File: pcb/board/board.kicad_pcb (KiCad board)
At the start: 2 copper layers, 100 x 34 mm, 68 parts, among them J1 USB_C_Receptacle_USB2.0, J3 Micro_SD_Card_Det, J4 Conn_01x05_Male, J6 Conn_02x02_Top_Bottom, J7 Screw_Terminal_Speaker, Q1 DMG2305UX, SW6 BOOTSEL, U2 BQ25172, U3 TLV61070A, U4 XC6206P332MR, U5 MAX98357, U6 RP2040, U7 W25Q128JVS, Y1 X322512MSB4SI

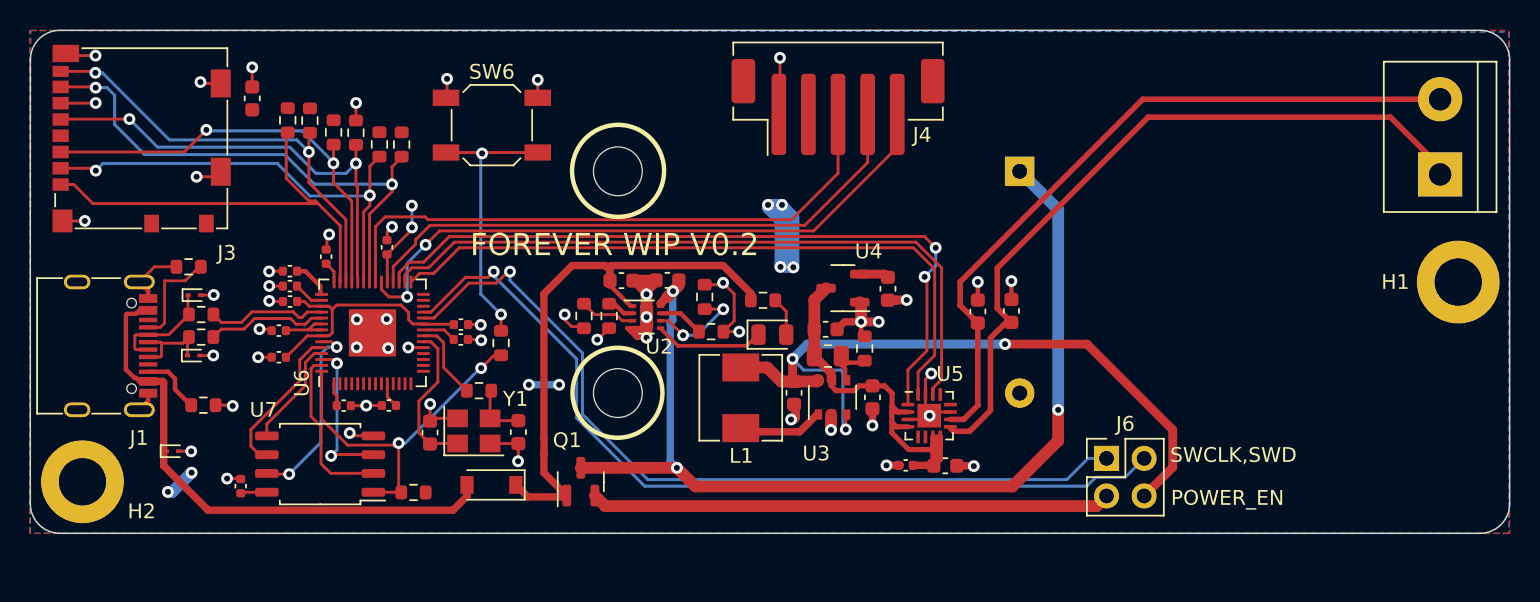
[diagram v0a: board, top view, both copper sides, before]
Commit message: Update readmes. Uncovered I2C bug :(
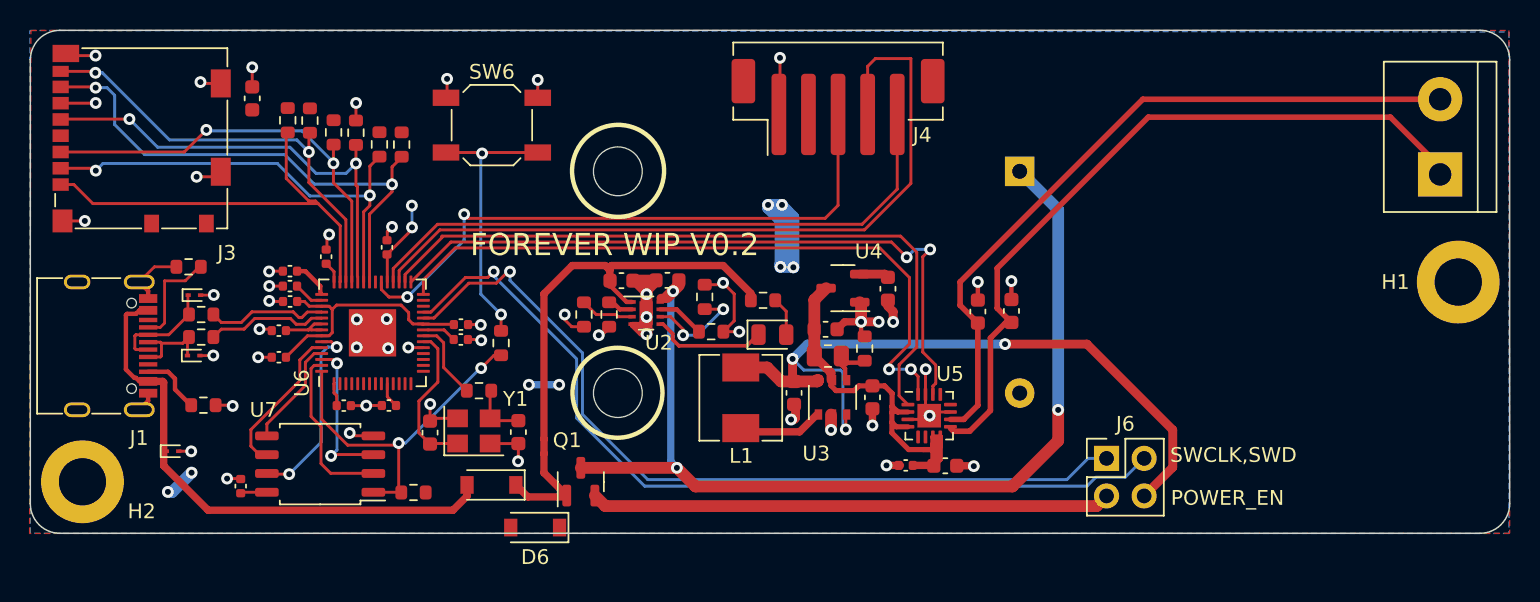
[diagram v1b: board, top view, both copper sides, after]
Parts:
- added D6: B5819W SL, Diode_SMD:D_SOD-123, F.Cu at (131.1, 91.6)
- moved U2 0.27 mm to (138.6, 77.1)
- moved R11 0.10 mm to (136.1, 77.2)
- moved R12 0.10 mm to (134.4, 77.2)
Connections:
- Q1 pad 1: Net-(C4-Pad1) -> Net-(Q1-Pad1)
- R13 pad 1: Net-(C4-Pad1) -> /USB_VBUS
- U6 pad 28: /rp2040/GPIO17 -> AMP_BCLK
- U6 pad 29: AMP_BCLK -> AMP_LRCLK
- U6 pad 30: AMP_LRCLK -> AMP_DIN
- U6 pad 31: AMP_DIN -> RP2040_SDA
- U6 pad 32: RP2040_SDA -> RP2040_SCL
- U6 pad 34: RP2040_SCL -> INT
- U6 pad 35: INT -> /rp2040/GPIO23
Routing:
- net RP2040_SDA: track 39.5 -> 52.6 mm
- net AMP_DIN: track 49.7 -> 47.7 mm, vias 2 -> 0
- net GND: track 91.4 -> 89.7 mm
- net RP2040_SCL: track 43.3 -> 42.3 mm, vias 2 -> 0
- net INT: track 40.6 -> 41.6 mm, vias 0 -> 2
- net AMP_BCLK: track 45.9 -> 45.7 mm, vias 0 -> 2
- net AMP_LRCLK: track 47.2 -> 47.3 mm, vias 0 -> 2

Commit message: Update readme and pcb
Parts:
- moved J7 21.1 mm to (171.2, 66.1)
- moved Q1 3.92 mm to (138.1, 88.6)
- moved D6 2.92 mm to (132.9, 89.3)
- moved D4 1.20 mm to (127.1, 89.3)
- moved C10 0.43 mm to (158.8, 87.0)
- moved C11 0.30 mm to (156.2, 87.1)
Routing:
- net /USB_VBUS: track 37.0 -> 66.8 mm, vias 0 -> 2
- net Net-(C12-Pad1): track 50.2 -> 26.6 mm
- net Net-(C13-Pad2): track 49.2 -> 29.7 mm
- net Net-(C4-Pad1): track 37.4 -> 25.1 mm
- net /Power/BAT_OR_USB_POWER_OUT: track 35.1 -> 31.2 mm
- net Net-(D6-Pad1): track 0.00 -> 2.85 mm
- net VDD: track 38.7 -> 40.2 mm
- net Net-(BT1-Pad1): track 67.2 -> 67.8 mm
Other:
- board text added: "+"
- board text added: "-"
- board text added: "FOREVER WIP V0.3"
- board text removed: "FOREVER WIP V0.2"

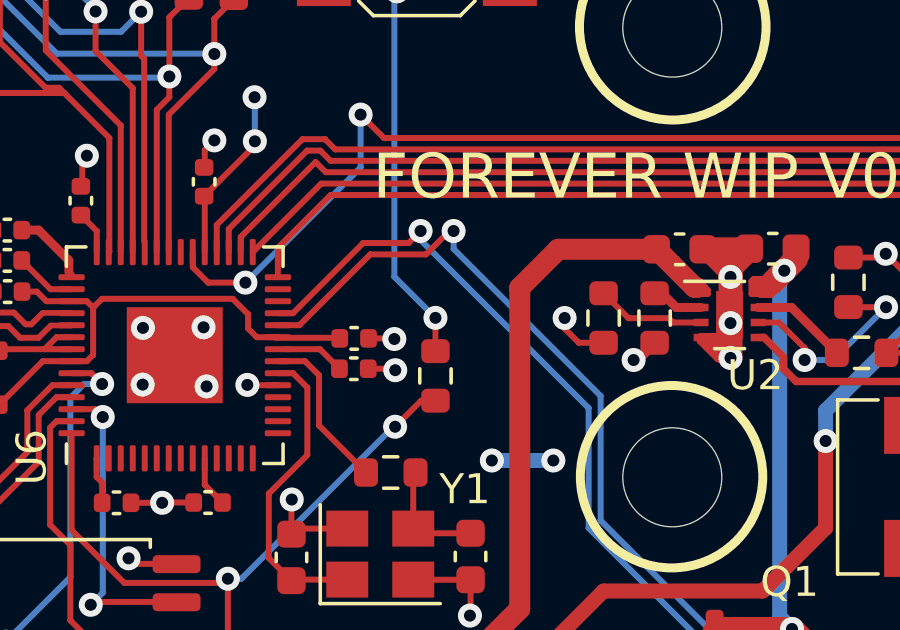
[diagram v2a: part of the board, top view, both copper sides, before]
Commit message: manually trigger sound and update the pcb layout
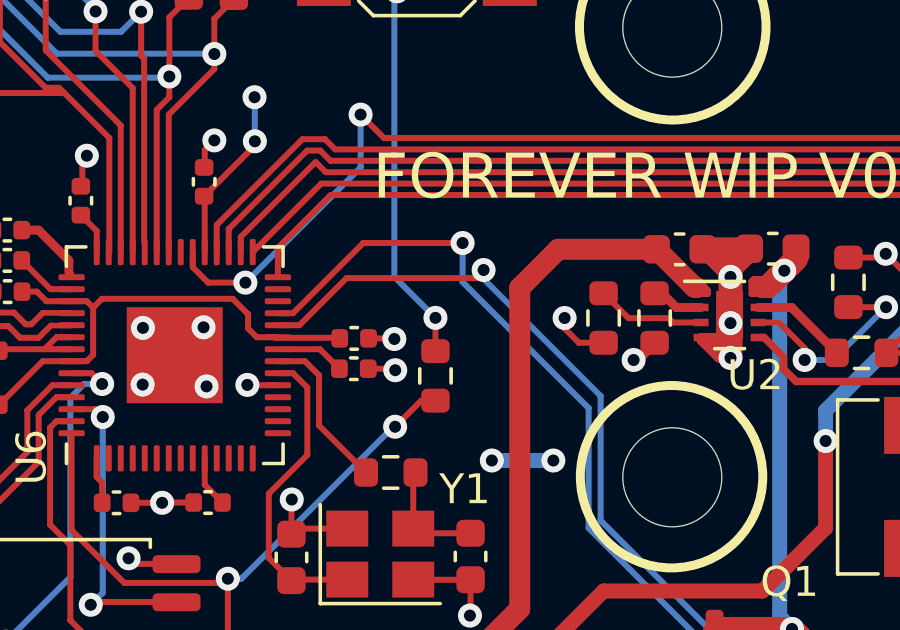
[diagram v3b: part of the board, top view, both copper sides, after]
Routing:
- net /rp2040/SWCLK: track 56.7 -> 55.4 mm
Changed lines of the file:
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@@
   (segment (start 155.024382 80.9) (end 155.0205 80.903882) (width 0.2) (layer "B.Cu") (net 48))
   (segment (start 124.26 77.44) (end 123.5425 77.44) (width 0.2) (layer "F.Cu") (net 51))
-  (segment (start 128.48 75.08) (end 126.62 75.08) (width 0.2) (layer "F.Cu") (net 51))
-  (segment (start 129.26 74.3) (end 128.48 75.08) (width 0.2) (layer "F.Cu") (net 51))
-  (segment (start 126.62 75.08) (end 124.26 77.44) (width 0.2) (layer "F.Cu") (net 51))
-  (segment (start 129.4 74.3) (end 129.26 74.3) (width 0.2) (layer "F.Cu") (net 51))
-  (via (at 129.4 74.3) (size 0.8) (drill 0.4) (layers "F.Cu" "B.Cu") (net 51))
+  (segment (start 125.82998 75.87002) (end 124.26 77.44) (width 0.2) (layer "F.Cu") (net 51))
+  (segment (start 130.4 75.6) (end 130.12998 75.87002) (width 0.2) (layer "F.Cu") (net 51))
+  (segment (start 130.12998 75.87002) (end 125.82998 75.87002) (width 0.2) (layer "F.Cu") (net 51))
+  (via (at 130.4 75.6) (size 0.8) (drill 0.4) (layers "F.Cu" "B.Cu") (net 51))
   (segment (start 138.71 88.36) (end 167.04 88.36) (width 0.2) (layer "B.Cu") (net 51))
-  (segment (start 129.4 74.896666) (end 134.3 79.796666) (width 0.2) (layer "B.Cu") (net 51))
-  (segment (start 129.4 74.3) (end 129.4 74.896666) (width 0.2) (layer "B.Cu") (net 51))
+  (segment (start 167.04 88.36) (end 168.475 86.925) (width 0.2) (layer "B.Cu") (net 51))
+  (segment (start 130.4 75.6) (end 130.4 75.896666) (width 0.2) (layer "B.Cu") (net 51))
   (segment (start 134.3 83.95) (end 138.71 88.36) (width 0.2) (layer "B.Cu") (net 51))
   (segment (start 168.475 86.925) (end 169.725 86.925) (width 0.2) (layer "B.Cu") (net 51))
   (segment (start 134.3 79.796666) (end 134.3 83.95) (width 0.2) (layer "B.Cu") (net 51))
-  (segment (start 167.04 88.36) (end 168.475 86.925) (width 0.2) (layer "B.Cu") (net 51))
+  (segment (start 130.4 75.896666) (end 134.3 79.796666) (width 0.2) (layer "B.Cu") (net 51))
+  (segment (start 124.04669 77.04) (end 123.5425 77.04) (width 0.2) (layer "F.Cu") (net 52))
   (segment (start 126.38669 74.7) (end 124.04669 77.04) (width 0.2) (layer "F.Cu") (net 52))
-  (segment (start 127.89904 74.7) (end 126.38669 74.7) (width 0.2) (layer "F.Cu") (net 52))
-  (segment (start 128.29952 74.29952) (end 127.89904 74.7) (width 0.2) (layer "F.Cu") (net 52))
-  (segment (start 124.04669 77.04) (end 123.5425 77.04) (width 0.2) (layer "F.Cu") (net 52))
-  (via (at 128.29952 74.29952) (size 0.8) (drill 0.4) (layers "F.Cu" "B.Cu") (net 52))
-  (segment (start 133.9 80.2) (end 133.9 84.2) (width 0.2) (layer "B.Cu") (net 52))
-  (segment (start 128.29952 74.29952) (end 128.29952 74.59952) (width 0.2) (layer "B.Cu") (net 52))
+  (segment (start 129.700322 74.7) (end 126.38669 74.7) (width 0.2) (layer "F.Cu") (net 52))
+  (via (at 129.700322 74.7) (size 0.8) (drill 0.4) (layers "F.Cu" "B.Cu") (net 52))
   (segment (start 169 88.2) (end 170.99 88.2) (width 0.2) (layer "B.Cu") (net 52))
   (segment (start 168.4 88.8) (end 169 88.2) (width 0.2) (layer "B.Cu") (net 52))
-  (segment (start 133.9 84.2) (end 138.5 88.8) (width 0.2) (layer "B.Cu") (net 52))
   (segment (start 170.99 88.2) (end 172.265 86.925) (width 0.2) (layer "B.Cu") (net 52))
   (segment (start 138.5 88.8) (end 168.4 88.8) (width 0.2) (layer "B.Cu") (net 52))
-  (segment (start 128.29952 74.59952) (end 133.9 80.2) (width 0.2) (layer "B.Cu") (net 52))
+  (segment (start 133.9 80.2) (end 133.9 84.2) (width 0.2) (layer "B.Cu") (net 52))
+  (segment (start 129.700322 74.7) (end 129.700322 76.000322) (width 0.2) (layer "B.Cu") (net 52))
+  (segment (start 133.9 84.2) (end 138.5 88.8) (width 0.2) (layer "B.Cu") (net 52))
+  (segment (start 129.700322 76.000322) (end 133.9 80.2) (width 0.2) (layer "B.Cu") (net 52))
   (segment (start 114.475 87.99) (end 113.168112 87.99) (width 0.2) (layer "F.Cu") (net 58))
   (segment (start 113.113112 87.935) (end 112.965 87.935) (width 0.2) (layer "F.Cu") (net 58))

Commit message: update pcb
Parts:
- added JP1: CHG_LED_EN, Jumper:SolderJumper-2_P1.3mm_Bridged_RoundedPad1.0x1.5mm, F.Cu at (143.7, 83.5)
- moved D5 14.8 mm to (138.8, 90.8), turned to 180 degrees
- moved U5 11.4 mm to (162.2, 73.5)
- moved C11 11.4 mm to (160.7, 76.6)
- moved C10 11.4 mm to (163.3, 76.5)
- moved C13 9.83 mm to (169.1, 71.4)
- moved C12 9.58 mm to (171.1, 71.4)
- moved R12 8.83 mm to (143.2, 77.6)
- moved R16 8.75 mm to (151.3, 76.4)
- moved U2 8.72 mm to (147.3, 77.5)
- moved C4 8.72 mm to (145.6, 75.3)
- moved C7 8.72 mm to (148.7, 75.3)
- moved R11 8.72 mm to (144.8, 77.6)
- moved R17 8.41 mm to (151.4, 78.8)
- moved Q1 5.91 mm to (144.0, 88.3)
- moved R13 5.29 mm to (144.0, 80.9)
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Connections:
- D5 pad 2: Net-(D5-Pad2) -> /USB_VBUS
- R13 pad 1: /USB_VBUS -> Net-(R13-Pad1)
- R13 pad 2: Net-(D5-Pad2) -> Net-(U2-Pad5)
- U2 pad 5: Net-(D5-Pad1) -> Net-(U2-Pad5)
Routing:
- net /USB_VBUS: track 66.8 -> 50.4 mm, vias 2 -> 0
- net Net-(C12-Pad1): track 26.6 -> 15.3 mm
- net Net-(C13-Pad2): track 29.7 -> 19.7 mm
- net +3.3V: track 44.6 -> 52.0 mm
- net Net-(C4-Pad1): track 25.1 -> 31.5 mm
- net /Power/BAT_OR_USB_POWER_OUT: track 31.2 -> 24.9 mm
- net Net-(BT1-Pad1): track 67.8 -> 61.8 mm
- net Net-(D6-Pad1): track 2.85 -> 8.43 mm
- net AMP_BCLK: track 45.4 -> 40.2 mm, vias 2 -> 0
- net Net-(U2-Pad5): track 0.00 -> 5.10 mm
- net VDD: track 40.2 -> 45.2 mm
- net /Power/BAT_OR_USB_POWER_IN: track 49.9 -> 45.7 mm
- net AMP_LRCLK: track 47.0 -> 42.9 mm, vias 2 -> 0
- net AMP_DIN: track 47.6 -> 44.0 mm, vias 0 -> 2
- net Net-(D5-Pad2): track 2.63 -> 0.00 mm
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
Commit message: pcb version 0.3
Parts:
- added JP2: CHARGE_CTRL, Jumper:SolderJumper-2_P1.3mm_Bridged_RoundedPad1.0x1.5mm, F.Cu at (141.2, 77.5)
- added JP3: V_SENSE_EN, Jumper:SolderJumper-2_P1.3mm_Bridged_RoundedPad1.0x1.5mm, F.Cu at (138.8, 87.9)
- added Q2: AO3400A, Package_TO_SOT_SMD:SOT-23, F.Cu at (138.0, 76.8)
- added R21: 10K, Resistor_SMD:R_0603_1608Metric, F.Cu at (141.5, 81.3)
- added R22: 27K, Resistor_SMD:R_0603_1608Metric, F.Cu at (135.5, 87.3)
- added R23: 27K, Resistor_SMD:R_0603_1608Metric, F.Cu at (174.6, 82.3)
- added SW1: PWR, Button_Switch_THT:SW_E-Switch_EG1224_SPDT_Angled, F.Cu at (176.5, 86.3)
- moved R8 6.07 mm to (111.3, 69.3)
- moved R3 3.64 mm to (112.9, 62.0), turned to 90 degrees
- moved C1 1.06 mm to (111.1, 62.0)
- moved J6 1.03 mm to (168.7, 87.0)
- moved JP1 0.60 mm to (144.3, 83.5)
- moved C24 0.56 mm to (121.1, 72.1)
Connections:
- J3 pad 1: SD_DAT2 -> Net-(J3-Pad1)
- J3 pad 8: SD_DAT1 -> Net-(J3-Pad8)
- R3 pad 2: SD_DAT1 -> Net-(J3-Pad8)
- R8 pad 2: SD_DAT2 -> Net-(J3-Pad1)
- U3 pad 3: /Power/BAT_OR_USB_POWER_IN -> Net-(U3-Pad3)
- U6 pad 40: SD_DAT1 -> CHARGE_EN
- U6 pad 41: SD_DAT2 -> V_SENSE
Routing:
- net V_SENSE: track 0.00 -> 45.0 mm, vias 0 -> 4
- net CHARGE_EN: track 0.00 -> 35.3 mm, vias 0 -> 4
- net SD_DAT1: track 31.0 -> 0.00 mm, vias 2 -> 0
- net SD_DAT2: track 30.5 -> 0.00 mm
- net Net-(U3-Pad3): track 0.00 -> 27.1 mm, vias 0 -> 2
- net Net-(J3-Pad8): track 0.00 -> 16.6 mm
- net Net-(J3-Pad1): track 0.00 -> 13.6 mm
- net Net-(BT1-Pad1): track 61.8 -> 68.7 mm, vias 3 -> 4
- net Net-(JP2-Pad1): track 0.00 -> 4.35 mm
- net GND: track 91.5 -> 95.2 mm, vias 52 -> 55
- net +3.3V: track 52.0 -> 48.7 mm, vias 10 -> 8
- net Net-(C4-Pad1): track 31.5 -> 34.3 mm
- net Net-(R12-Pad2): track 3.67 -> 5.72 mm
- net Net-(JP3-Pad2): track 0.00 -> 2.02 mm
- net /Power/BAT_OR_USB_POWER_IN: track 45.7 -> 46.8 mm, vias 3 -> 2
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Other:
- board text added: "CHR_CTRL"
- board text added: "CHR_LED"
- board text added: "ON/OFF"
- board text added: "V_SENSE"

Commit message: pcb v0.3
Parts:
- added JP4: Jumper_2_Bridged, Jumper:SolderJumper-2_P1.3mm_Bridged_RoundedPad1.0x1.5mm, F.Cu at (176.6, 81.3)
- moved R23 5.39 mm to (179.9, 81.3)
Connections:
- R23 pad 1: Net-(U3-Pad3) -> Net-(JP4-Pad1)
- SW1 pad 1: Net-(U3-Pad3) -> Net-(JP4-Pad2)
- U3 pad 3: Net-(U3-Pad3) -> Net-(JP4-Pad2)
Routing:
- net Net-(JP4-Pad2): track 0.00 -> 28.7 mm, vias 0 -> 2
- net Net-(U3-Pad3): track 27.1 -> 0.00 mm, vias 2 -> 0
- net Net-(JP4-Pad1): track 0.00 -> 1.88 mm
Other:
- board text added: "PWR_EN_PULLDOWN"
